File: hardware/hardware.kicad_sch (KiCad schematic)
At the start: 61 parts, among them J1 RUN OUT, J2 USB_C_Receptacle_USB2.0, J3 MIDI IN, J4 MIDI OUT, J5 Eurorack_Power, J6 CV1, J7 CV2, J8 CV3, J9 CV4, Q1 NPN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

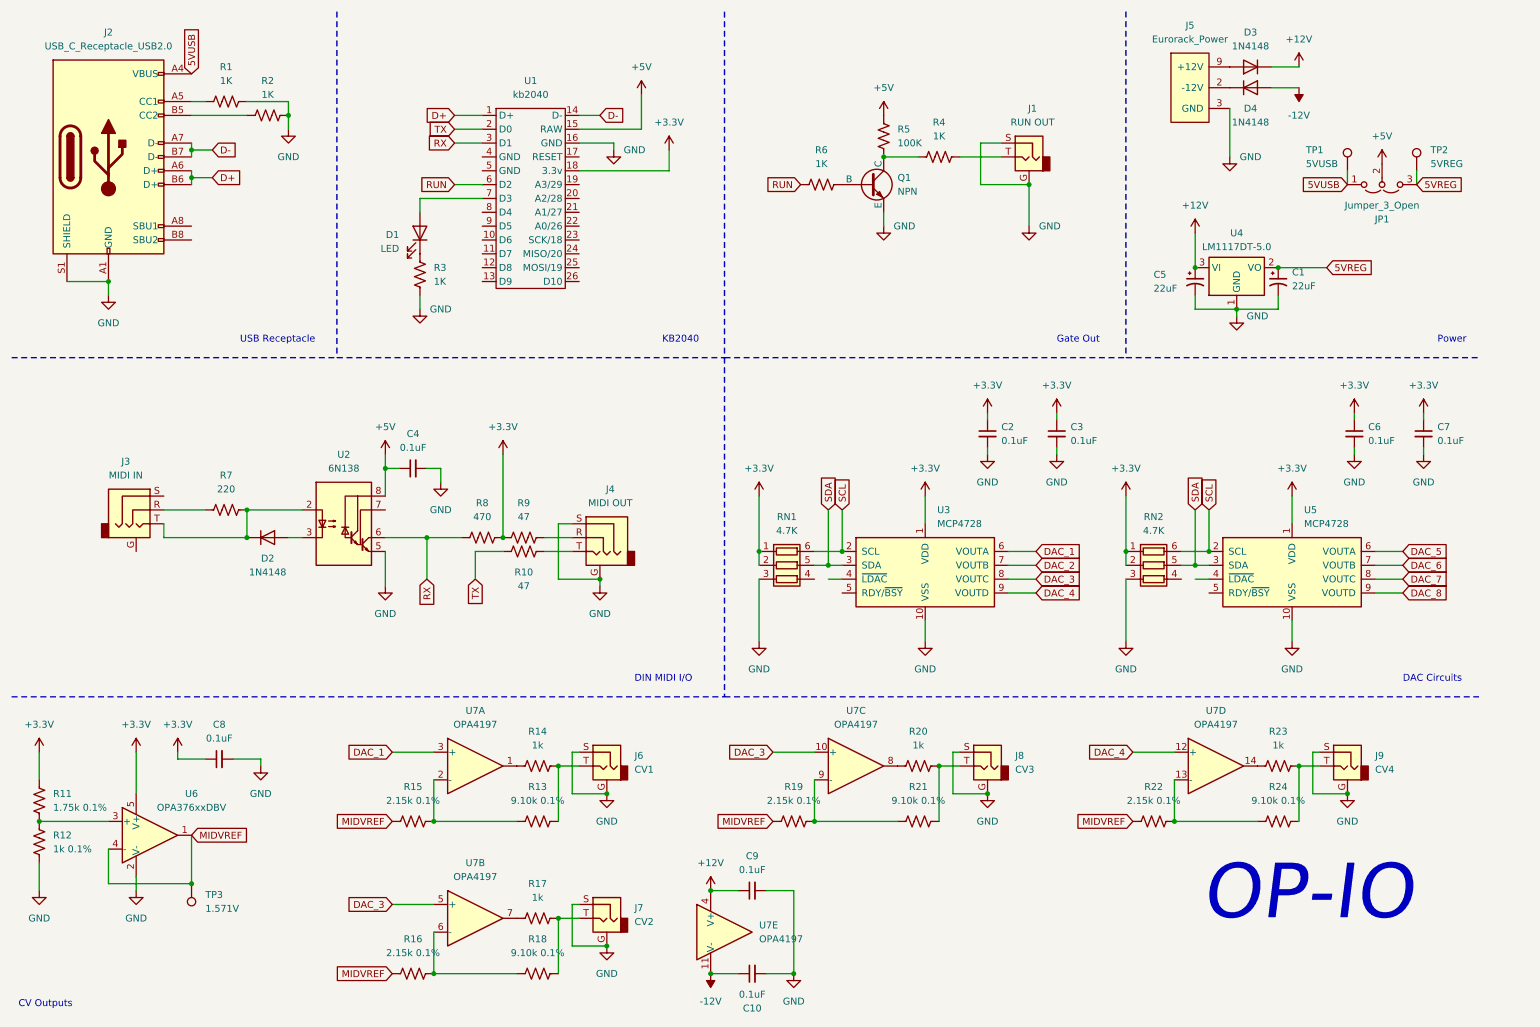
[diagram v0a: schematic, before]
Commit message: finished initial PCB layout
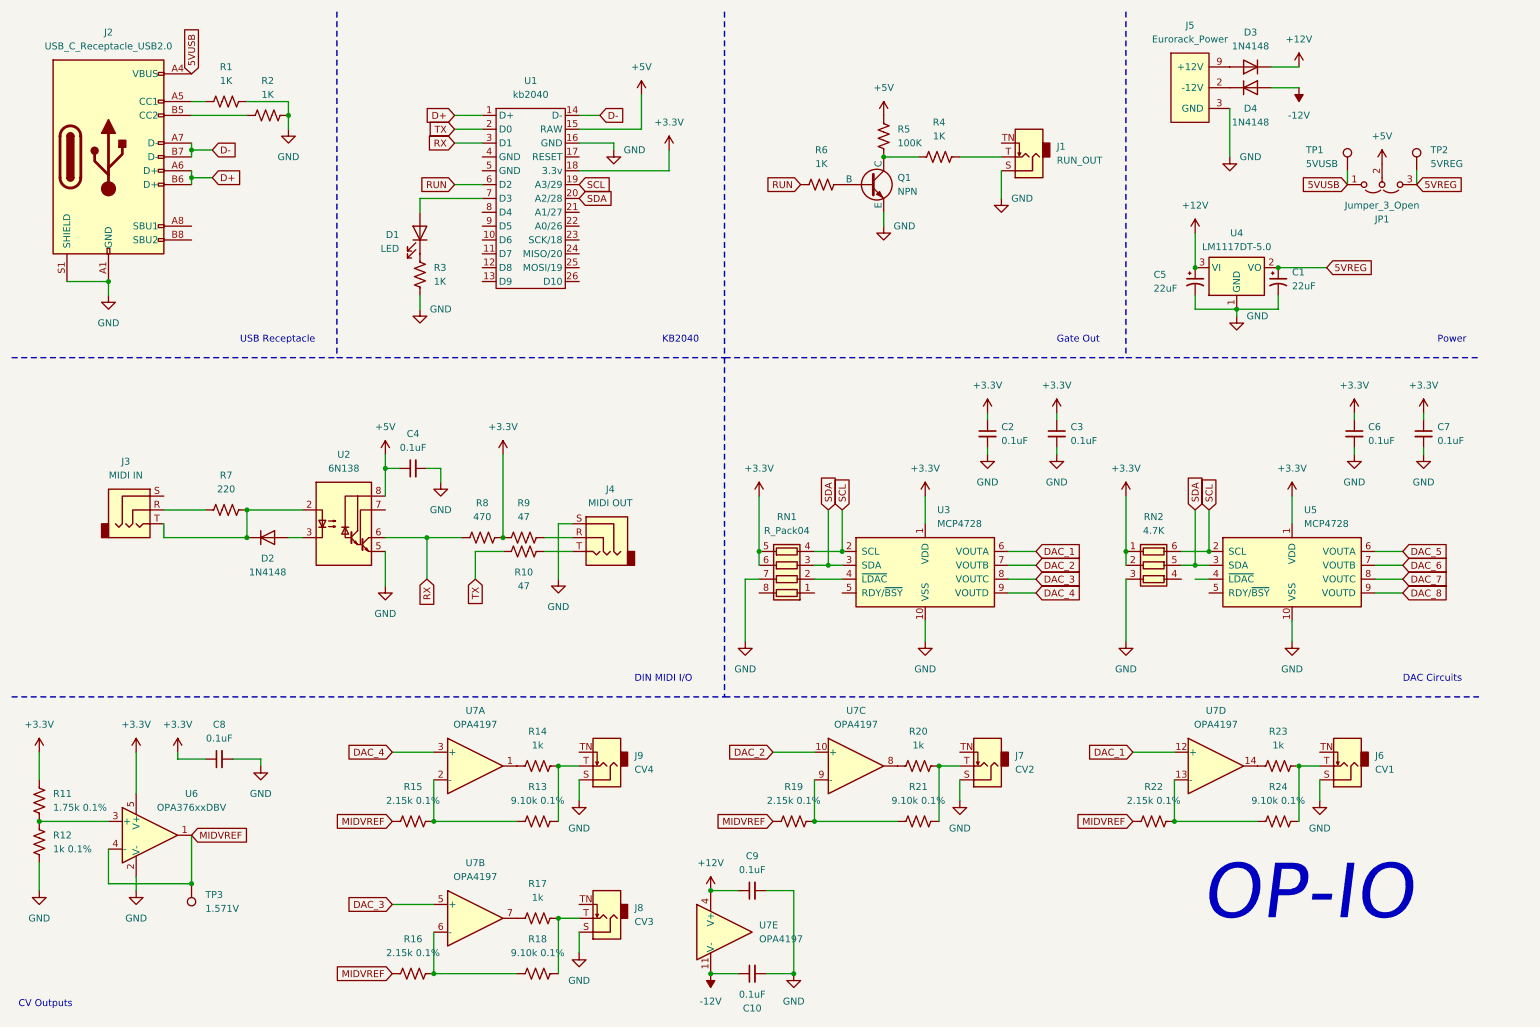
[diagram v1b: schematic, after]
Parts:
- removed J1: RUN OUT, symbol Connector_Audio:AudioJack2_Ground
- removed J6: CV1, symbol Connector_Audio:AudioJack2_Ground
- removed J7: CV2, symbol Connector_Audio:AudioJack2_Ground
- removed J8: CV3, symbol Connector_Audio:AudioJack2_Ground
- removed J9: CV4, symbol Connector_Audio:AudioJack2_Ground
- removed RN1: 4.7K, symbol Device:R_Pack03
- added J1: RUN_OUT, winterbloom:AudioJack_WQP518MA, symbol winterbloom:Eurorack_Mono_Jack
- added J6: CV1, winterbloom:AudioJack_WQP518MA, symbol winterbloom:Eurorack_Mono_Jack
- added J7: CV2, winterbloom:AudioJack_WQP518MA, symbol winterbloom:Eurorack_Mono_Jack
- added J8: CV3, winterbloom:AudioJack_WQP518MA, symbol winterbloom:Eurorack_Mono_Jack
- added J9: CV4, winterbloom:AudioJack_WQP518MA, symbol winterbloom:Eurorack_Mono_Jack
- added RN1: R_Pack04, Resistor_SMD:R_Array_Convex_4x0612, symbol Device:R_Pack04
- C1, C5: footprint (none) -> Capacitor_SMD:CP_Elec_6.3x7.7
- C10, C2, C3, C4, C6, C7, C8, C9: footprint (none) -> Capacitor_SMD:C_0805_2012Metric
- D1: footprint (none) -> LED_THT:LED_D3.0mm_FlatTop
- D2, D3, D4: footprint Diode_THT:D_DO-35_SOD27_P7.62mm_Horizontal -> winterbloom:D_SOD-123
- J2: footprint (none) -> Connector_USB:USB_C_Receptacle_GCT_USB4115-03-C
- J3, J4: footprint (none) -> AudioJacks:Jack_3.5mm_QingPu_WQP-PJ366ST_Vertical
- JP1: footprint (none) -> Jumper:SolderJumper-3_P1.3mm_Open_Pad1.0x1.5mm
- Q1: footprint (none) -> Package_TO_SOT_SMD:SOT-23-3
- R1, R10, R11, R12, R13, R14, R15, R16, R17, R18, R19, R2, R20, R21, R22, R23, R24, R3, R4, R5, R6, R7, R8, R9: footprint (none) -> winterbloom:R_0805_HandSolder
- RN2: footprint (none) -> Resistor_SMD:R_Array_Convex_4x1206
- TP1, TP2, TP3: footprint (none) -> TestPoint:TestPoint_Pad_D2.5mm
- U1: footprint (none) -> kb2040:kb2040
- U2: footprint (none) -> Package_DIP:SMDIP-8_W9.53mm
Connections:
- net +3.3V: now also RN1.5 (R4.2), RN1.6 (R3.2)
- net DAC_1: now also U7.12 (+); no longer U7.3 (+)
- net DAC_2: now also U7.10 (+)
- net DAC_3: no longer U7.10 (+)
- net DAC_4: now also U7.3 (+); no longer U7.12 (+)
- net GND: now also J1.S (Sleeve), J6.S (Sleeve), J7.S (Sleeve), J8.S (Sleeve), J9.S (Sleeve), RN1.7 (R2.2); no longer J4.G
- net SCL: now also U1.19 (A3/29), RN1.4 (R4.1)
- net SDA: now also U1.20 (A2/28), RN1.3 (R3.1)
- net at R13.2, R14.2: now also J9.T (Tip)
- net at R4.2: now also J1.T (Tip)
- net at R23.2, R24.2: now also J6.T (Tip)
- net at R17.2, R18.2: now also J8.T (Tip)
- net at R20.2, R21.2: now also J7.T (Tip)
- net at U3.4 (~{LDAC}): now also RN1.2 (R2.1)

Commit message: ready for fab
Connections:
- net RUN: now also U1.23 (SCK/18); no longer U1.6 (D2)
- net at D1.2 (A): now also U1.13 (D9); no longer U1.7 (D3)
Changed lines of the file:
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@@
+    (stroke (width 0) (type default))
+  )
+  (wire (pts (xy 95.25 62.23) (xy 100.33 62.23))
     (stroke (width 0) (type default))
   )
@@
     (stroke (width 0) (type default))
   )
+  (wire (pts (xy 88.9 46.99) (xy 95.25 46.99))
+    (stroke (width 0) (type default))
+  )
   (wire (pts (xy 196.85 116.84) (xy 201.93 116.84))
     (stroke (width 0) (type default))
@@
     (stroke (width 0) (type default))
   )
-  (wire (pts (xy 95.25 44.45) (xy 100.33 44.45))
-    (stroke (width 0) (type default))
-  )
   (wire (pts (xy 46.99 43.18) (xy 50.8 43.18))
     (stroke (width 0) (type default))
@@
     (stroke (width 0) (type default))
   )
+  (wire (pts (xy 95.25 46.99) (xy 95.25 62.23))
+    (stroke (width 0) (type default))
+  )
   (wire (pts (xy 118.11 34.29) (xy 129.54 34.29))
     (stroke (width 0) (type default))
@@
   )
   (wire (pts (xy 64.77 31.75) (xy 64.77 34.29))
-    (stroke (width 0) (type default))
-  )
-  (wire (pts (xy 88.9 46.99) (xy 100.33 46.99))
     (stroke (width 0) (type default))
   )
@@
     )
   )
-  (global_label "RUN" (shape input) (at 95.25 44.45 180) (fields_autoplaced)
-    (effects (font (size 1.27 1.27)) (justify right))
-    (property "Intersheetrefs" "${INTERSHEET_REFS}" (at 88.3338 44.45 0)
-      (effects (font (size 1.27 1.27)) (justify right) hide)
-    )
-  )
+  (global_label "RUN" (shape input) (at 118.11 54.61 0) (fields_autoplaced)
+    (effects (font (size 1.27 1.27)) (justify left))
+    (property "Intersheetrefs" "${INTERSHEET_REFS}" (at 125.0262 54.61 0)
+      (effects (font (size 1.27 1.27)) (justify left) hide)
+    )
+  )
